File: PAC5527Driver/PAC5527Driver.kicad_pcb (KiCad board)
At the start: 4 copper layers, 27.5 x 27.5 mm, 80 parts, among them J1 Conn_01x08, J2 Conn_01x04, J3 Conn_01x04, J4 Conn_01x02, U1 USBLC6-2SC6, U2 SN65HVD230, U3 MA730, U4 PAC5527, U5 HT7550-1-SOT89

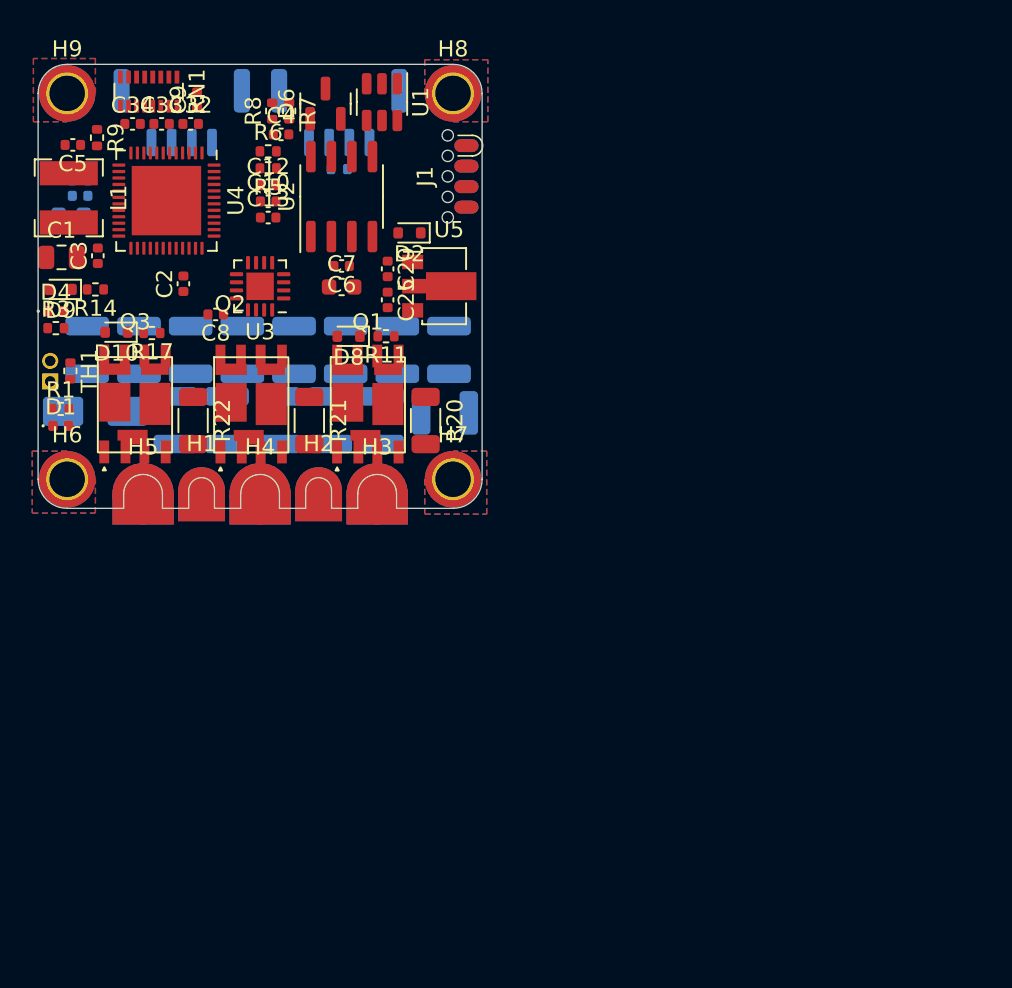
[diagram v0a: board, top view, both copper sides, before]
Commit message: relocated to align encoder with board geometric center
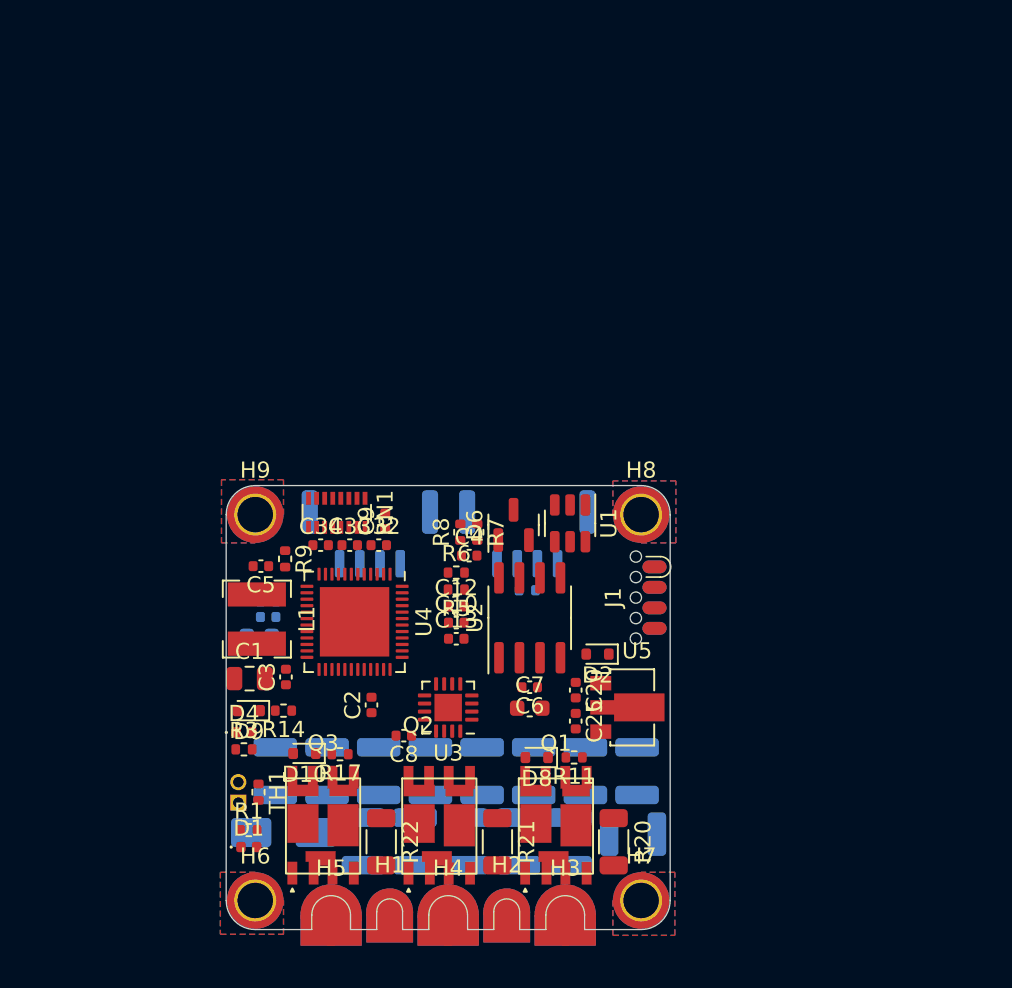
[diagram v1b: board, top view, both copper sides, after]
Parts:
- moved C10 28.6 mm to (105.9, 114.6)
- moved C11 28.6 mm to (94.2, 113.3)
- moved C12 28.6 mm to (105.9, 113.6)
- moved C13 28.6 mm to (105.9, 115.6)
- moved C16 28.6 mm to (93.7, 115.4)
- moved C18 28.6 mm to (94.2, 114.2)
- moved C2 28.6 mm to (100.7, 119.7)
- moved C22 28.6 mm to (97.9, 123.8)
- moved C23 28.6 mm to (94.7, 123.8)
- moved C29 28.6 mm to (110.7, 123.8)
- moved C30 28.6 mm to (107.5, 123.8)
- moved C34 28.6 mm to (97.5, 109.8)
- moved C39 28.6 mm to (113.9, 123.8)
- moved C4 28.6 mm to (106.7, 110.4)
- moved C6 28.6 mm to (110.5, 118.6)
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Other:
- outline, holes or cut-outs redrawn

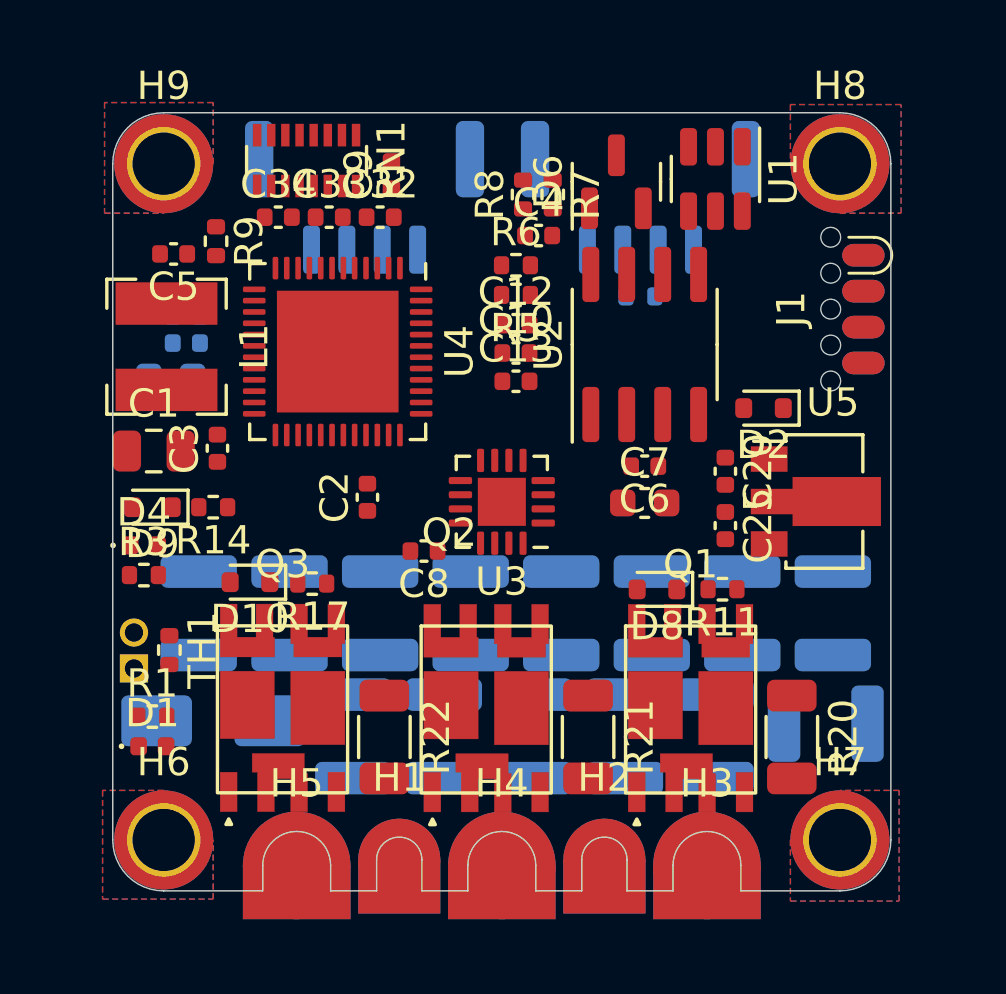
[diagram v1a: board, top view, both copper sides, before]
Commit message: MCU fanout, power stage roughed in, setup is now 6L
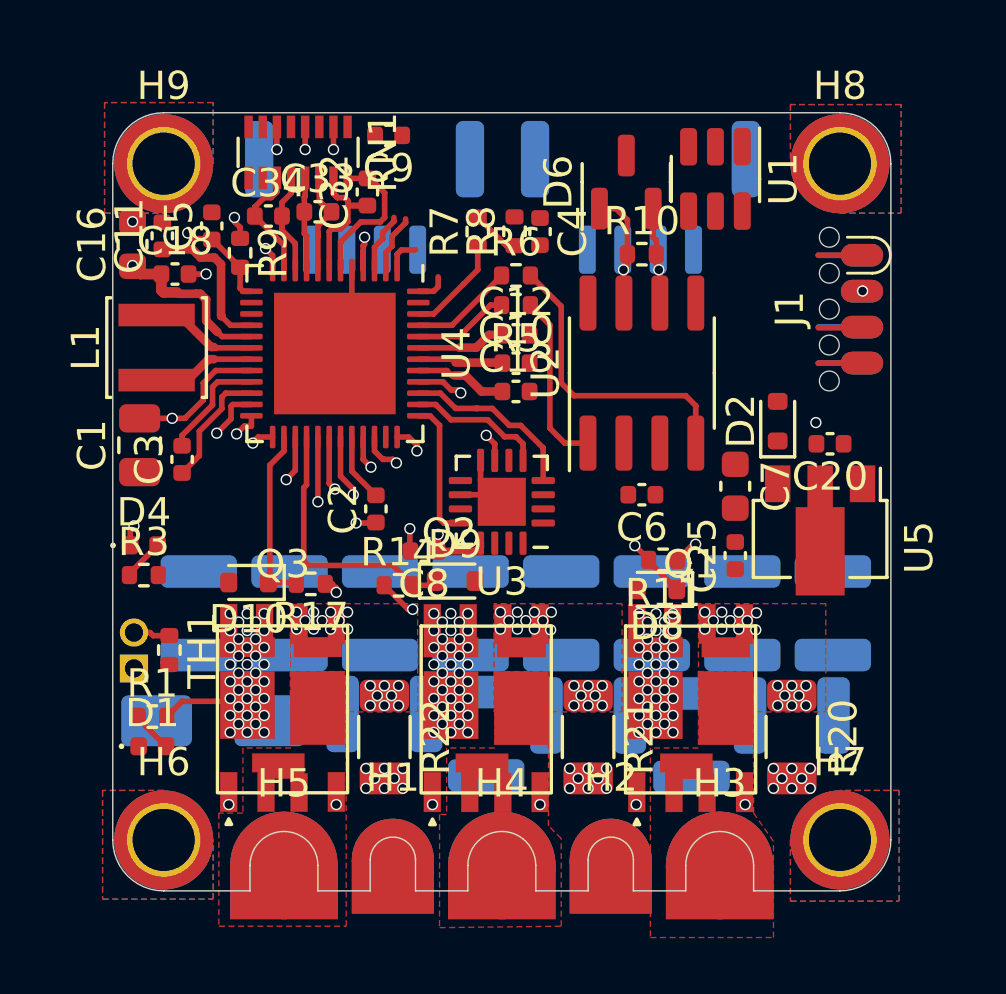
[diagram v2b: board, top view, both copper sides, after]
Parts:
- removed C15: 10uF, Capacitor_SMD:C_1210_3225Metric
- C11, C16, C18, R10: moved to F.Cu
- L1: footprint Inductor_SMD:L_Bourns-SRN4018 -> Inductor_SMD:L_Changjiang_FNR3010S
- moved D9 11.0 mm to (103.8, 122.6), turned to 0 degrees
- moved C27 8.54 mm to (101.2, 127.3), turned to 180 degrees
- moved R14 7.11 mm to (101.8, 122.8), turned to 0 degrees
- moved C16 4.88 mm to (92.3, 110.7), turned to 90 degrees
- moved C20 3.83 mm to (117.0, 117.8), turned to 180 degrees
- moved C7 3.25 mm to (113.7, 119.3), turned to -90 degrees
- moved C11 2.96 mm to (93.4, 110.4), turned to 90 degrees
- moved R7 2.96 mm to (104.5, 110.3), turned to 90 degrees
- moved C18 2.47 mm to (93.8, 111.8), turned to 0 degrees
- moved R11 2.34 mm to (111.1, 121.9)
- moved C24 2.04 mm to (108.5, 127.4), turned to 180 degrees
- moved C5 1.67 mm to (95.2, 110.1), turned to 90 degrees
- moved C17 1.50 mm to (104.8, 128.0)
- moved R10 1.49 mm to (110.3, 111.1)
- moved C9 1.39 mm to (101.4, 106.9), turned to 180 degrees
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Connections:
- J1 pad 5: /SWDIO -> /EXT_UART_TX
- J1 pad 6: GND -> /EXT_UART_RX
- J1 pad 7: /EXT_UART_TX -> GND
- J1 pad 8: /EXT_UART_RX -> /SWDIO
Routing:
- net Net-(U2-R): track 0.00 -> 10.7 mm
- net /VS: track 0.00 -> 9.50 mm
- net VDC: track 0.00 -> 9.11 mm, vias 0 -> 116
- net GND: track 0.00 -> 7.96 mm, vias 0 -> 28
- net /ENC_MOSI: track 0.00 -> 6.48 mm
- net /WS: track 0.00 -> 6.35 mm
- net /AIO1: track 0.00 -> 6.28 mm
- net Net-(U2-D): track 0.00 -> 6.20 mm
- net Net-(U4A-VSYS): track 0.00 -> 5.33 mm
- net /AIO0: track 0.00 -> 5.32 mm
- net +12V: track 0.00 -> 5.00 mm, vias 0 -> 2
- net /ENC_SCLK: track 0.00 -> 4.99 mm
- net /ENC_CS0: track 0.00 -> 4.86 mm
- net /NTC_IN: track 0.00 -> 4.83 mm, vias 0 -> 1
- net /AIO2: track 0.00 -> 4.56 mm
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- added copper zone on F.Cu, net /UOUT
- added copper zone on F.Cu, net /VOUT
- added copper zone on F.Cu, net /WOUT
- added copper zone on F.Cu, net Net-(RN1B-R2.1)
- added copper zone on In1.Cu, net Net-(RN1B-R2.1)
- added copper zone on F.Cu, net Net-(RN1D-R4.1)
- added copper zone on In1.Cu, net Net-(RN1D-R4.1)
- added copper zone on F.Cu, net Net-(RN1F-R6.1)
- added copper zone on In1.Cu, net Net-(RN1F-R6.1)
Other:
- outline, holes or cut-outs redrawn
- copper layers 4 -> 6

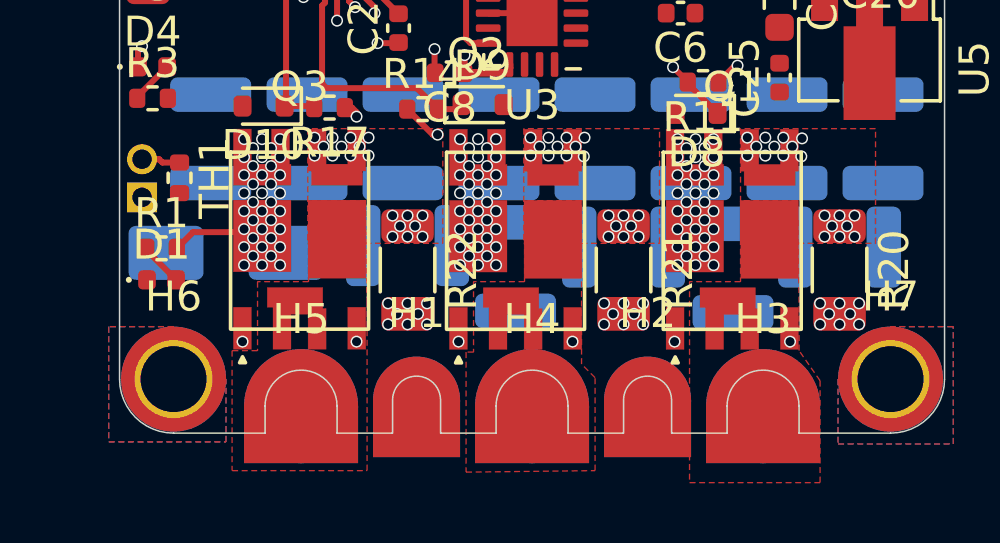
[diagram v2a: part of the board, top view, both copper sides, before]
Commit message: output via stitching
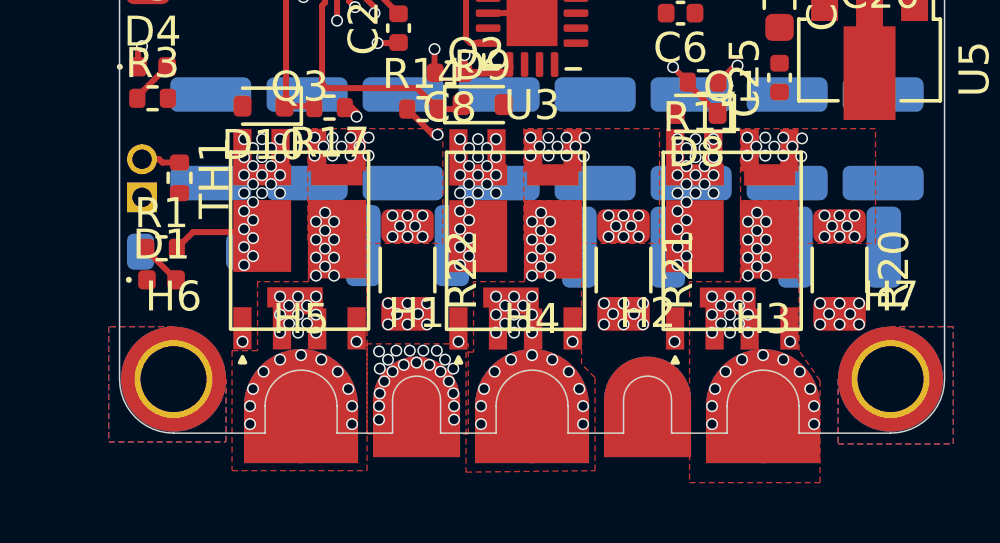
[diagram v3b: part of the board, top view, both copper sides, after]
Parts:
- removed C17, C28: 10uF, Capacitor_SMD:C_1210_3225Metric
- D3: footprint Diode_SMD:D_SMA -> Diode_SMD:D_SOD-123
- moved D3 1.20 mm to (94.0, 127.5)
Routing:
- net VDC: vias 116 -> 102
- net /WOUT: vias 1 -> 37
- net /VOUT: vias 1 -> 37
- net /UOUT: vias 1 -> 37
- added copper zone on In1.Cu, net /UOUT
- added copper zone on In2.Cu, net /UOUT
- added copper zone on In1.Cu, net /VOUT
- added copper zone on In2.Cu, net /VOUT
- added copper zone on In1.Cu, net /WOUT
- added copper zone on In2.Cu, net /WOUT
- added copper zone on In2.Cu, net Net-(RN1B-R2.1)
- added copper zone on In2.Cu, net Net-(RN1D-R4.1)
- added copper zone on In2.Cu, net Net-(RN1F-R6.1)
- added copper zone on F.Cu, net VDC

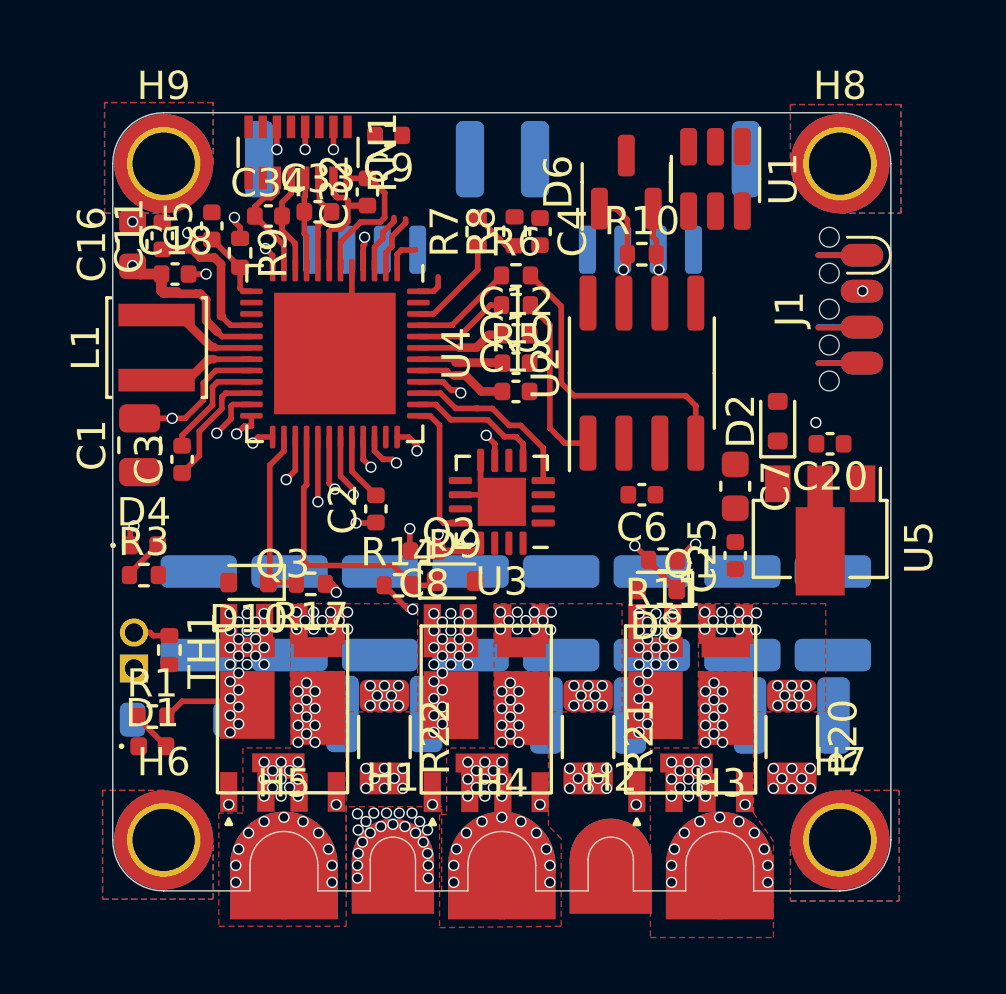
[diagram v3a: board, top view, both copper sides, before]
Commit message: VCC / GND pours
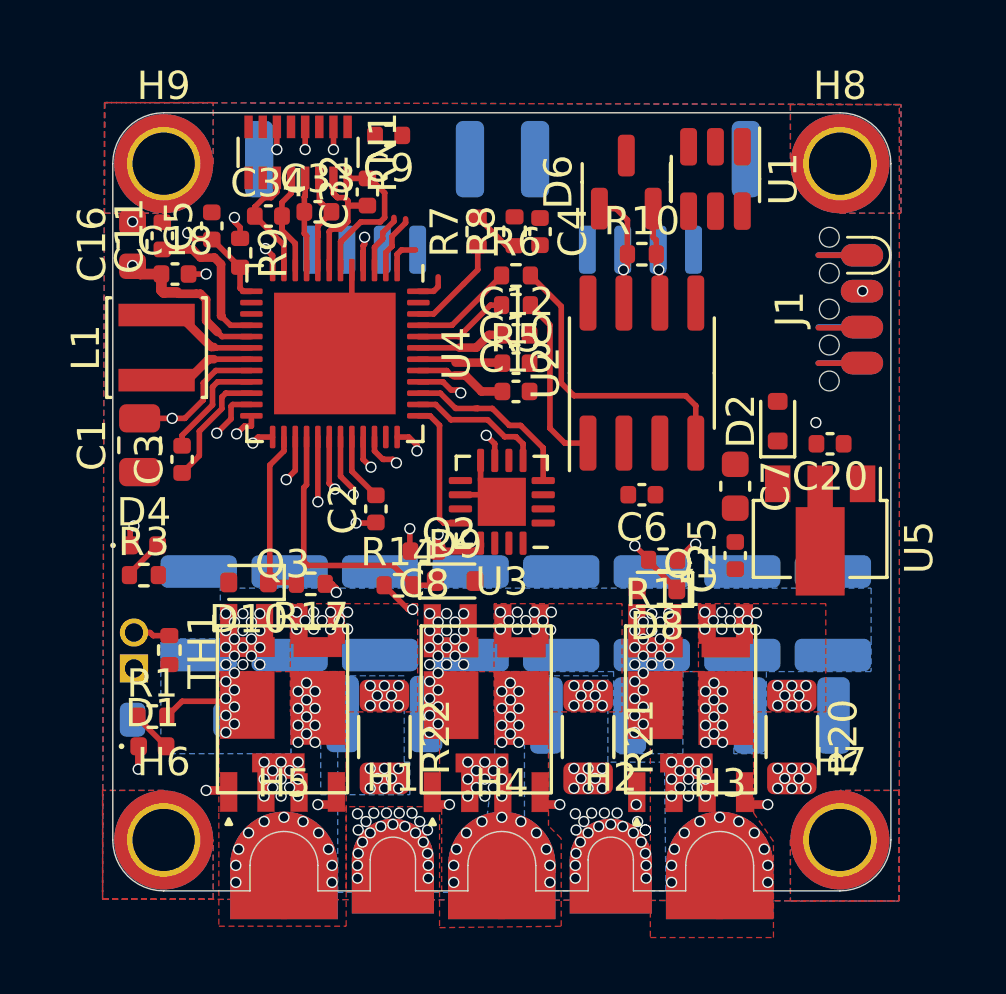
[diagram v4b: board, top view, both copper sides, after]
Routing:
- net /VOUT: track 1.36 -> 7.87 mm
- net /UOUT: track 0.87 -> 6.82 mm
- net /WOUT: track 0.87 -> 6.79 mm
- net GND: track 7.96 -> 8.77 mm, vias 28 -> 51
- net /WH: track 1.64 -> 2.43 mm
- net /WL: track 1.87 -> 2.63 mm
- net /VL: track 1.00 -> 1.76 mm
- net /UL: track 0.78 -> 1.53 mm
- net /VH: track 2.24 -> 2.89 mm
- added copper zone on B.Cu, net VDC
- added copper zone on In4.Cu, net VDC

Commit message: initial layout pass
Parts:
- C7: footprint Capacitor_SMD:C_0603_1608Metric -> Capacitor_SMD:C_0402_1005Metric
- R10: moved to B.Cu
- R20, R21, R22: footprint Resistor_SMD:R_1206_3216Metric -> PAC5527Driver:RShunt_1206_3216Metric
- moved R8 9.00 mm to (114.1, 106.6), turned to 0 degrees
- moved U1 8.00 mm to (105.0, 107.9), turned to 0 degrees
- moved C25 7.92 mm to (110.0, 114.7), turned to 0 degrees
- moved C4 7.82 mm to (114.0, 107.5), turned to 180 degrees
- moved U2 4.98 mm to (109.8, 110.3)
- moved C20 4.86 mm to (113.0, 115.1), turned to 0 degrees
- moved D6 4.66 mm to (114.2, 110.2), turned to 180 degrees
- moved U5 4.27 mm to (114.0, 117.8), turned to 0 degrees
- moved D2 4.22 mm to (113.4, 113.2)
- moved C7 3.70 mm to (110.0, 119.4), turned to 0 degrees
- moved C6 3.67 mm to (110.0, 115.9)
- moved C13 2.03 mm to (107.8, 116.7)
- moved C10 2.01 mm to (107.8, 115.6)
- moved R7 1.84 mm to (105.9, 111.5), turned to 0 degrees
- moved R10 1.70 mm to (110.3, 112.8)
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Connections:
- Q1 pad SL: Net-(RN1B-R2.1) -> Net-(Q1-PadSL)
- Q2 pad SL: Net-(RN1D-R4.1) -> Net-(Q2-PadSL)
- Q3 pad SL: Net-(RN1F-R6.1) -> Net-(Q3-PadSL)
- R20 pad 1: Net-(RN1B-R2.1) -> Net-(Q1-PadSL)
- R20 pad 2: GND -> Net-(RN1B-R2.1)
- R21 pad 1: Net-(RN1D-R4.1) -> Net-(Q2-PadSL)
- R21 pad 2: GND -> Net-(RN1D-R4.1)
- R22 pad 1: Net-(RN1F-R6.1) -> Net-(Q3-PadSL)
- R22 pad 2: GND -> Net-(RN1F-R6.1)
- RN1 pad 1: GND -> Net-(RN1A-R1.1)
- RN1 pad 3: GND -> Net-(RN1C-R3.1)
- RN1 pad 5: GND -> Net-(RN1E-R5.1)
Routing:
- net VDD: track 2.22 -> 43.9 mm, vias 1 -> 5
- net /UL: track 1.53 -> 41.1 mm
- net Net-(RN1A-R1.1): track 0.00 -> 34.3 mm, vias 0 -> 2
- net Net-(RN1E-R5.1): track 0.00 -> 32.8 mm, vias 0 -> 2
- net /PBTN: track 2.39 -> 34.9 mm, vias 1 -> 2
- net Net-(RN1F-R6.1): track 0.80 -> 33.0 mm, vias 20 -> 2
- net /VL: track 1.76 -> 33.0 mm
- net Net-(RN1C-R3.1): track 0.00 -> 30.8 mm, vias 0 -> 2
- net Net-(RN1B-R2.1): track 0.80 -> 31.0 mm, vias 20 -> 2
- net Net-(RN1D-R4.1): track 0.80 -> 28.2 mm, vias 20 -> 2
- net +12V: track 5.00 -> 29.4 mm
- net /UH: track 2.18 -> 23.8 mm
- net /CAN_H: track 4.14 -> 25.7 mm
- net /CAN_L: track 3.43 -> 24.0 mm
- net VDC: track 9.11 -> 28.9 mm, vias 102 -> 100
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- added copper zone on In3.Cu, net GND
- added copper zone on In4.Cu, net GND
- added copper zone on F.Cu, net Net-(Q1-PadSL)
- added copper zone on In1.Cu, net Net-(Q1-PadSL)
- added copper zone on In2.Cu, net Net-(Q1-PadSL)
- added copper zone on F.Cu, net Net-(Q2-PadSL)
- added copper zone on In1.Cu, net Net-(Q2-PadSL)
- added copper zone on In2.Cu, net Net-(Q2-PadSL)
- added copper zone on F.Cu, net Net-(Q3-PadSL)
- added copper zone on In1.Cu, net Net-(Q3-PadSL)
- added copper zone on In2.Cu, net Net-(Q3-PadSL)
- removed copper zone on F.Cu, net Net-(RN1B-R2.1)
- removed copper zone on In1.Cu, net Net-(RN1B-R2.1)
- removed copper zone on In2.Cu, net Net-(RN1B-R2.1)
- removed copper zone on F.Cu, net Net-(RN1D-R4.1)
- removed copper zone on In1.Cu, net Net-(RN1D-R4.1)
- removed copper zone on In2.Cu, net Net-(RN1D-R4.1)
- removed copper zone on F.Cu, net Net-(RN1F-R6.1)
- removed copper zone on In1.Cu, net Net-(RN1F-R6.1)
- removed copper zone on In2.Cu, net Net-(RN1F-R6.1)
